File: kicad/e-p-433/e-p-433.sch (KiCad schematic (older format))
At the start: 48 parts, among them P1 CONN_01X02, P2 CONN_01X02, P3 Transmitter, P4 ant, P5 Batterie, SW1 SWITCH_INV, SW2 SW_PUSH_m, SW3 Capuchon vert, U1 AD8495ARMZ, U2 AD8495ARMZ, U3 Teensy_3-2, U4 MCP_73831

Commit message: Modifier Sp.bak
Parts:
- removed W2: T2, Sp:Measurement_Point_Square-SMD-Pad_Big, symbol TEST_1P
- added W3: T1, Sp:Measurement_Point_Square-SMD-Pad_Big, symbol TEST_1P
- renumbered D3 to D2, D2 to D3, P4 to P3, P5 to P4, P3 to P5, R9 to R11, R11 to R12, R12 to R13, R13 to R15, R15 to R16, R16 to R17, R17 to R18, R18 to R7, R7 to R8, R8 to R9, SW3 to SW1, SW1 to SW3, W7 to W1, W1 to W2, W3 to W4, W4 to W5, W5 to W6, W6 to W7
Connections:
- wire segments 92 -> 98
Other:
- note added: "CI CMS e-p-433"
- note removed: "e-p-433"
- moved on the sheet: C1, C2, P1, R1, R3, R4, R7, SW1, SW2, U1, W1, W2

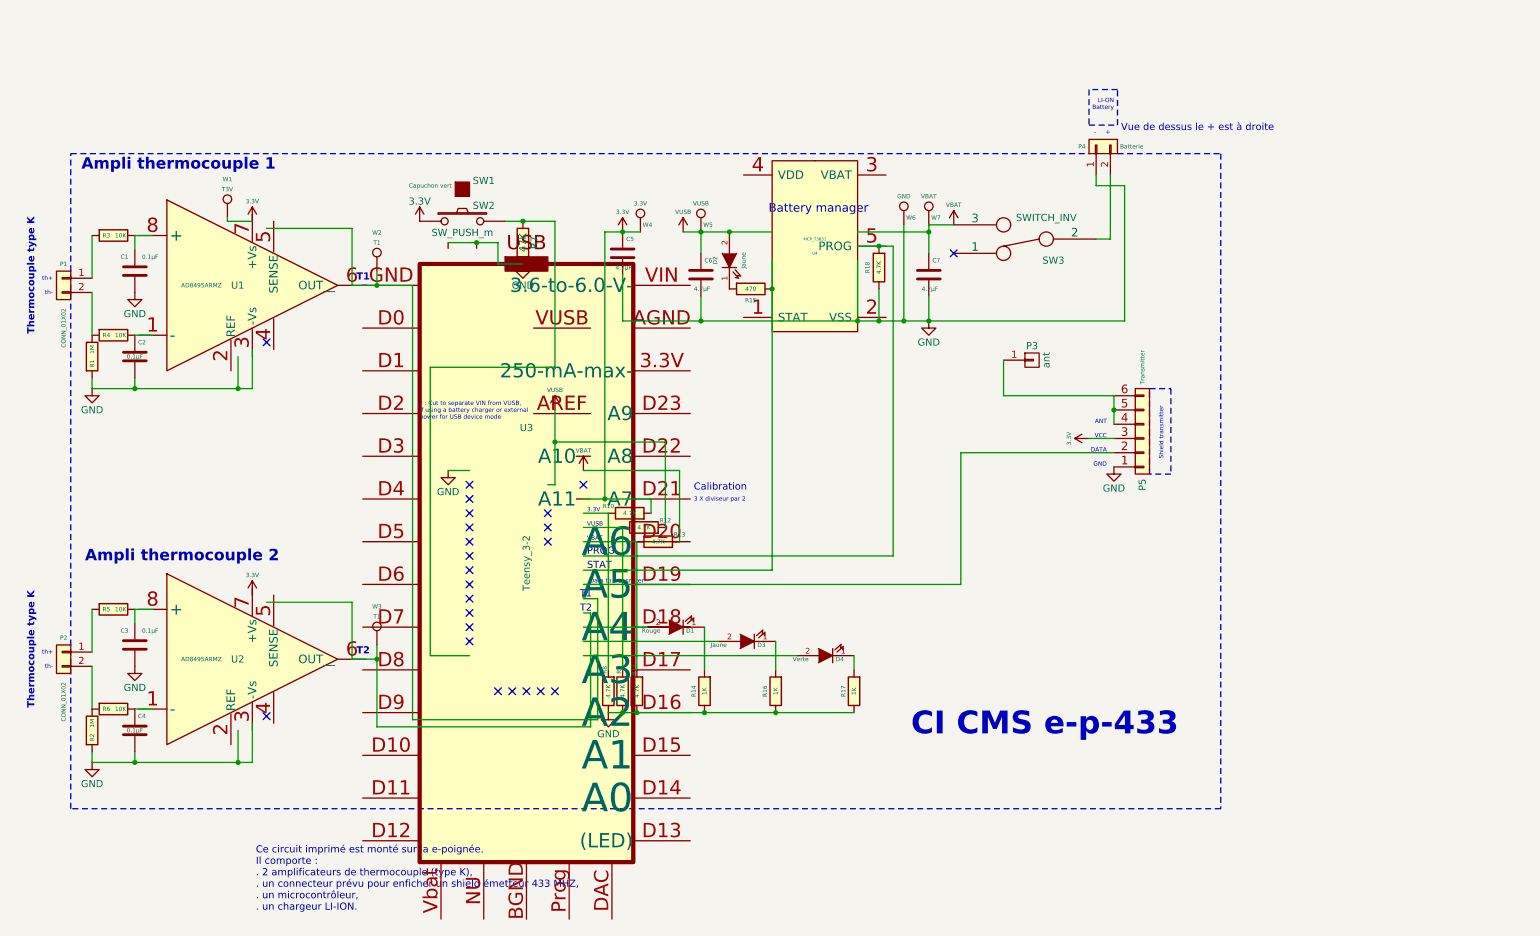
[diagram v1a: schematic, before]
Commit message: Modifier Sp et 8 fichiers e-p-433
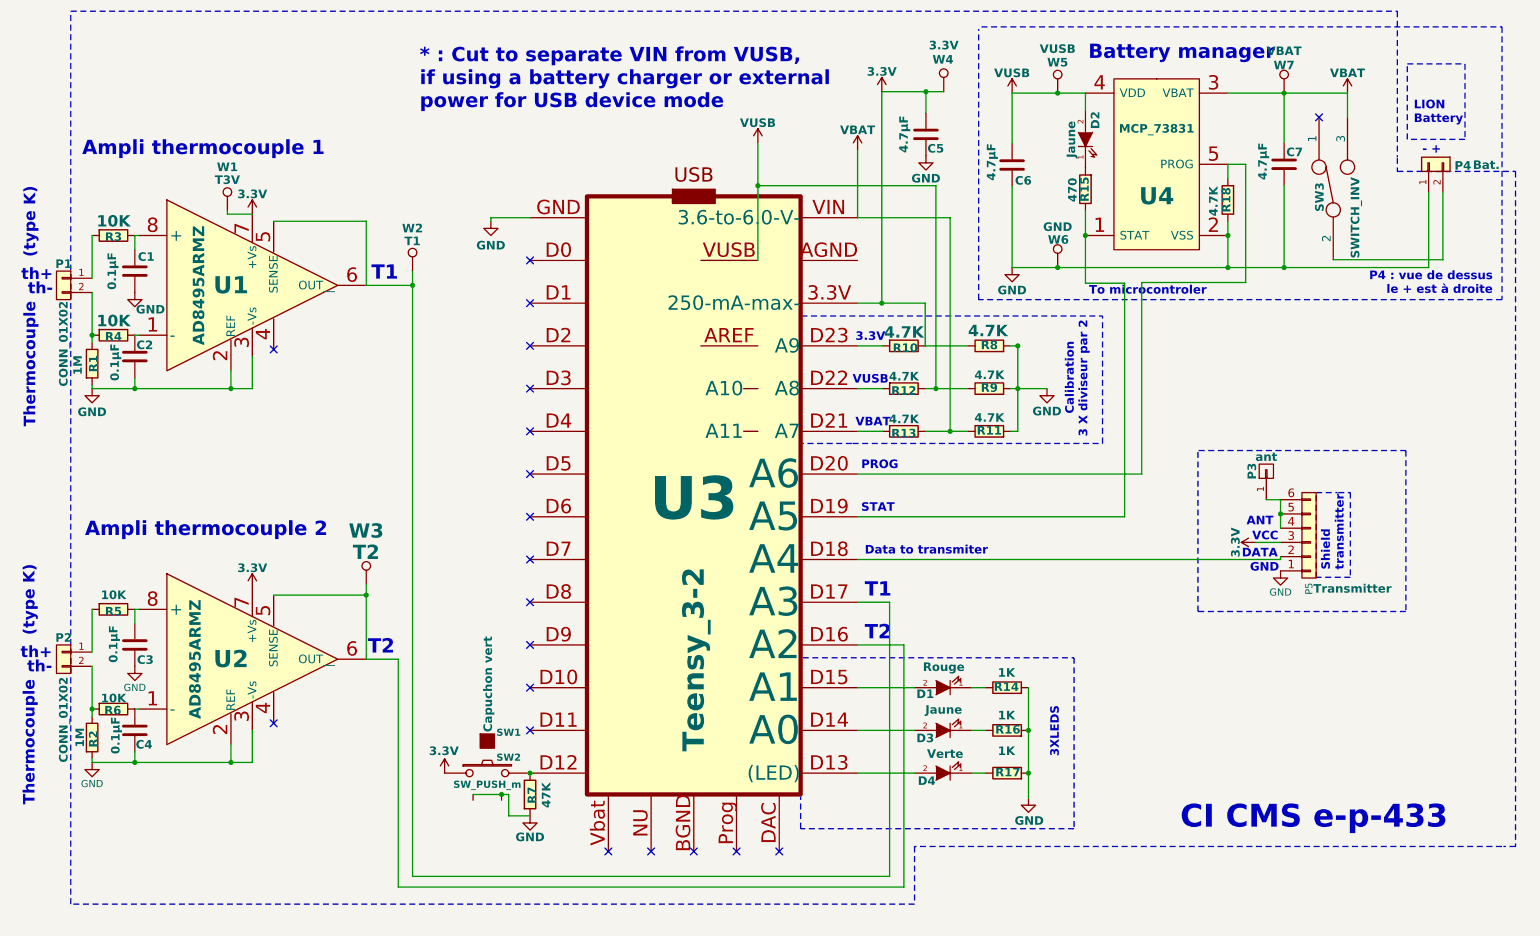
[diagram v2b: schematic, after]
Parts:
- P4: value Batterie -> Bat.
- W3: value T1 -> T2
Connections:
- wire segments 98 -> 97
- no-connect marks 24 -> 20
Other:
- note added: "(type K)"
- note added: "- +"
- note added: "3XLEDS"
- note added: "LION\nBattery"
- note added: "P4 : vue de dessus\nle + est à droite"
- note added: "Shield\ntransmitter"
- note added: "Thermocouple"
- note added: "To microcontroler"
- note removed: "+"
- note removed: "-"
- note removed: "Ce circuit imprimé est monté sur la e-poignée.\nIl comporte : \n. 2 amplificateurs de thermocouple (type K),\n. un connecteur prévu pour enficher un shield émetteur 433 MHZ,\n. un microcontrôleur,\n. un chargeur LI-ION."
- note removed: "LI-ON\nBattery"
- note removed: "Shield transmitter"
- note removed: "Thermocouple type K"
- note removed: "Vue de dessus le + est à droite"
- moved on the sheet: C5, C6, C7, D1, D2, D3, D4, P3, P4, P5, R1, R10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
